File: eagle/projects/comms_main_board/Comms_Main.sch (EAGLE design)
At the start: 93 parts, among them J1 RECE-20279-001E, J2 PRT-12639, J3 PRT-12639, J4 PRT-12639, J5 PRT-12639, Q1 CSD17579Q3A, U1 TPS562209DDCT, U11 TPS562209DDCT, U2 LP2985-33DBVR, U3 LP5900TLX-3.3/NOPB, U4 TPS562209DDCT, U5 LMZ34002RKGR, U6 LM3488MMX/NOPB, U7 PCT2075D,118, U8 MS560702BA03-50, U9 MAX-M8Q

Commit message: Started comms connectors portion of schematic
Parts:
- added J6: MOL-KK-3P-RA, daqcs:MOLKK_3PIN_3RA_RA
- added J7: MOL-KK-5P-V, daqcs:MOLKK_5PIN_5RA_RA
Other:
- note added: "APRS I2C Connector"
- note added: "COMMS Connectors"
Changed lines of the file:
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@@
 <part name="R14" library="daqcs" deviceset="RES" device="_0603" technology="_0R0" value="0"/>
 <part name="R15" library="daqcs" deviceset="RES" device="_0603" technology="_0R0" value="0"/>
+<part name="J6" library="daqcs" deviceset="MOLKK_3PIN" device="_RA" technology="_3RA" value="MOL-KK-3P-RA"/>
+<part name="SUPPLY14" library="supply2" deviceset="GND" device=""/>
+<part name="J7" library="daqcs" deviceset="MOLKK_5PIN" device="_RA" technology="_5RA" value="MOL-KK-5P-V"/>
+<part name="SUPPLY15" library="supply2" deviceset="GND" device=""/>
 </parts>
 <sheets>
@@
 <sheet>
 <plain>
+<text x="-30.226" y="84.328" size="5.08" layer="91">COMMS Connectors</text>
+<text x="-110.49" y="46.99" size="1.778" layer="91">APRS I2C Connector</text>
 </plain>
 <instances>
 <instance part="FRAME7" gate="G$1" x="-129.54" y="-83.82"/>
+<instance part="J6" gate="G$1" x="-106.68" y="63.5"/>
+<instance part="SUPPLY14" gate="GND" x="-88.9" y="53.34"/>
+<instance part="J7" gate="G$1" x="-60.96" y="58.42"/>
+<instance part="SUPPLY15" gate="GND" x="-40.64" y="40.64"/>
 </instances>
 <busses>
 </busses>
 <nets>
+<net name="N$51" class="0">
+<segment>
+<wire x1="-94.234" y1="58.42" x2="-88.9" y2="58.42" width="0.1524" layer="91"/>
+<wire x1="-88.9" y1="58.42" x2="-88.9" y2="55.626" width="0.1524" layer="91"/>
+</segment>
+</net>
+<net name="SCL" class="0">
+<segment>
+<wire x1="-94.234" y1="63.5" x2="-81.026" y2="63.5" width="0.1524" layer="91"/>
+<label x="-91.44" y="63.5" size="1.778" layer="95"/>
+</segment>
+</net>
+<net name="SDA" class="0">
+<segment>
+<wire x1="-94.234" y1="68.58" x2="-81.026" y2="68.58" width="0.1524" layer="91"/>
+<label x="-91.44" y="68.58" size="1.778" layer="95"/>
+</segment>
+</net>
+<net name="GND" class="0">
+<segment>
+<pinref part="SUPPLY15" gate="GND" pin="GND"/>
+<wire x1="-48.768" y1="48.26" x2="-40.64" y2="48.26" width="0.1524" layer="91"/>
+<wire x1="-40.64" y1="48.26" x2="-40.64" y2="43.18" width="0.1524" layer="91"/>
+</segment>
+</net>
+<net name="MOSI" class="0">
+<segment>
+<wire x1="-48.768" y1="53.34" x2="-35.56" y2="53.34" width="0.1524" layer="91"/>
+<label x="-45.72" y="53.34" size="1.778" layer="95"/>
+</segment>
+</net>
+<net name="MISO" class="0">
+<segment>
+<wire x1="-49.022" y1="58.42" x2="-35.56" y2="58.42" width="0.1524" layer="91"/>
+<label x="-45.72" y="58.42" size="1.778" layer="95"/>
+</segment>
+</net>
+<net name="SCLK" class="0">
+<segment>
+<wire x1="-48.514" y1="63.5" x2="-35.56" y2="63.5" width="0.1524" layer="91"/>
+<label x="-45.72" y="63.5" size="1.778" layer="95"/>
+</segment>
+</net>
+<net name="SS" class="0">
+<segment>
+<wire x1="-48.514" y1="68.58" x2="-35.814" y2="68.58" width="0.1524" layer="91"/>
+<label x="-45.72" y="68.58" size="1.778" layer="95"/>
+</segment>
+</net>
 </nets>
 </sheet>

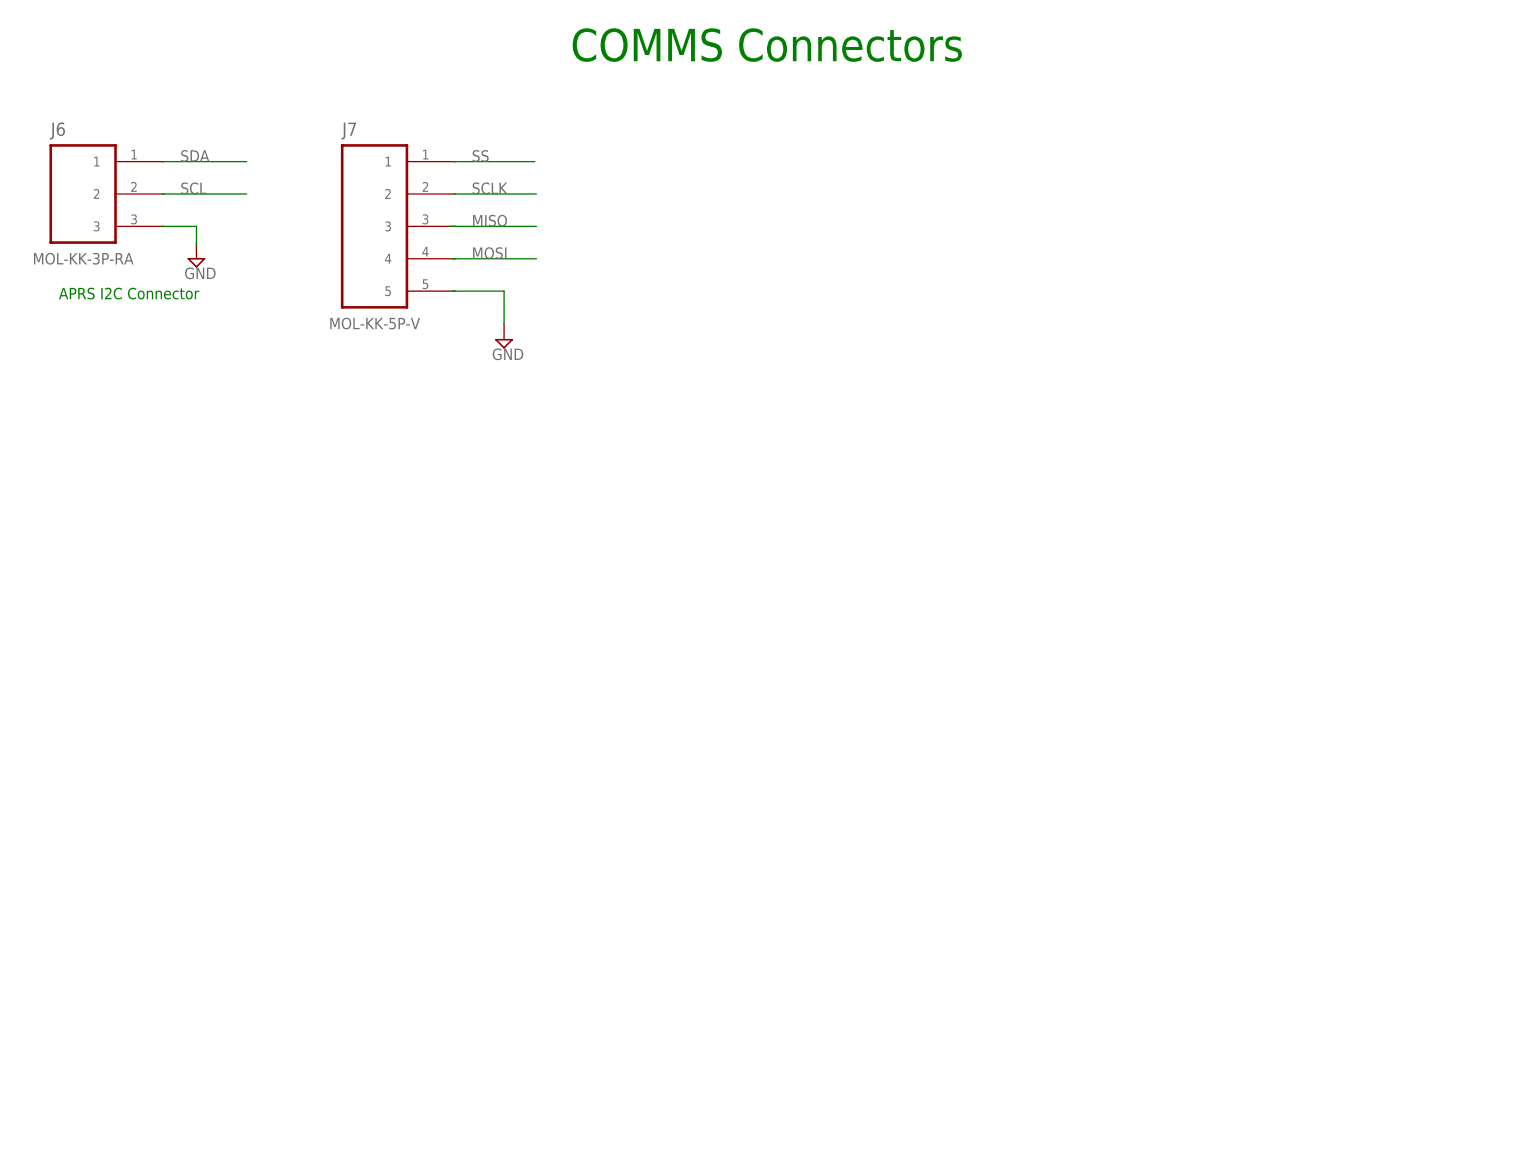
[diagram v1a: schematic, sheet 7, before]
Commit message: Added pi zero connector to schematic
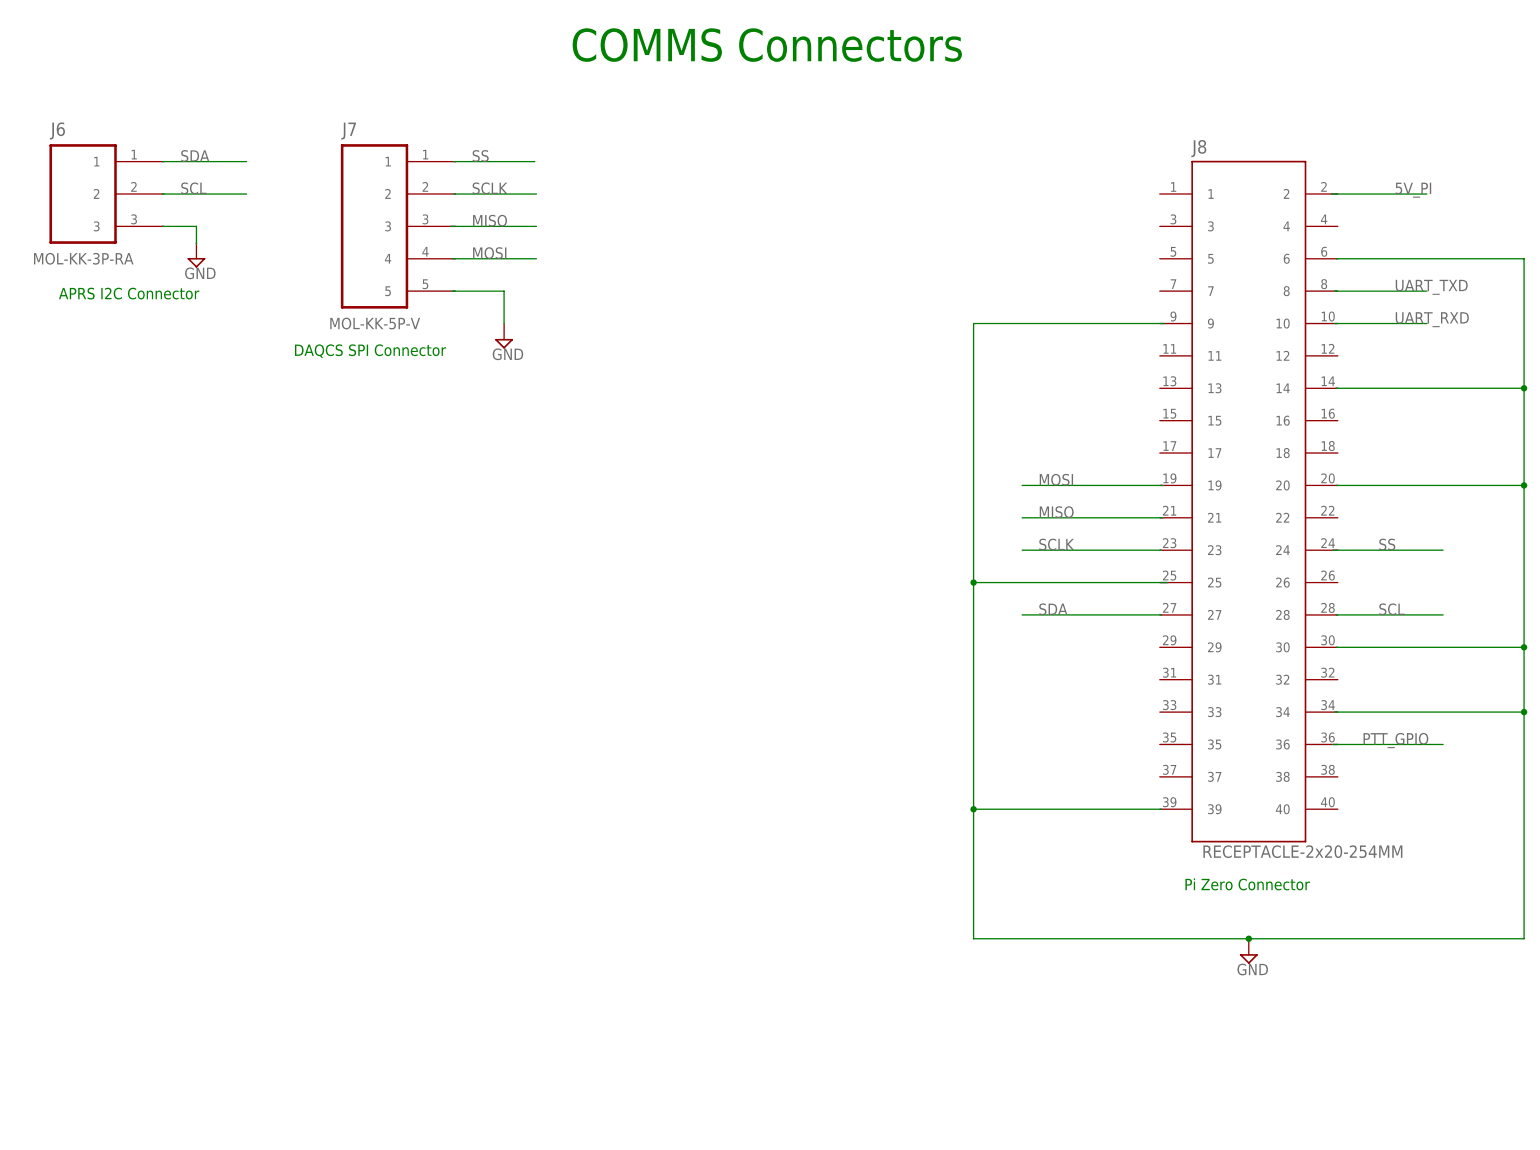
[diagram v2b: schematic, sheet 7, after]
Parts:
- added J8: RECEPTACLE-2x20-254MM, comms:RECEPTACLE-2X20-254MM
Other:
- note added: "DAQCS SPI Connector"
- note added: "Pi Zero Connector"
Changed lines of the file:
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@@
 <part name="J7" library="daqcs" deviceset="MOLKK_5PIN" device="_RA" technology="_5RA" value="MOL-KK-5P-V"/>
 <part name="SUPPLY15" library="supply2" deviceset="GND" device=""/>
+<part name="J8" library="comms" deviceset="RECEPTACLE-2X20-254MM" device="" value="RECEPTACLE-2x20-254MM"/>
+<part name="SUPPLY16" library="supply2" deviceset="GND" device=""/>
 </parts>
 <sheets>
@@
 <text x="-30.226" y="84.328" size="5.08" layer="91">COMMS Connectors</text>
 <text x="-110.49" y="46.99" size="1.778" layer="91">APRS I2C Connector</text>
+<text x="-73.66" y="38.1" size="1.778" layer="91">DAQCS SPI Connector</text>
+<text x="66.04" y="-45.72" size="1.778" layer="91">Pi Zero Connector</text>
 </plain>
 <instances>
@@
 <instance part="J7" gate="G$1" x="-60.96" y="58.42"/>
 <instance part="SUPPLY15" gate="GND" x="-40.64" y="40.64"/>
+<instance part="J8" gate="G$1" x="76.2" y="12.7"/>
+<instance part="SUPPLY16" gate="GND" x="76.2" y="-55.88"/>
 </instances>
 <busses>
@@
 <label x="-91.44" y="63.5" size="1.778" layer="95"/>
 </segment>
+<segment>
+<wire x1="89.916" y1="-2.54" x2="106.68" y2="-2.54" width="0.1524" layer="91"/>
+<label x="96.52" y="-2.54" size="1.778" layer="95"/>
+</segment>
 </net>
 <net name="SDA" class="0">
@@
 <wire x1="-94.234" y1="68.58" x2="-81.026" y2="68.58" width="0.1524" layer="91"/>
 <label x="-91.44" y="68.58" size="1.778" layer="95"/>
+</segment>
+<segment>
+<wire x1="62.484" y1="-2.54" x2="40.64" y2="-2.54" width="0.1524" layer="91"/>
+<label x="43.18" y="-2.54" size="1.778" layer="95"/>
 </segment>
 </net>
@@
 <wire x1="-40.64" y1="48.26" x2="-40.64" y2="43.18" width="0.1524" layer="91"/>
 </segment>
+<segment>
+<wire x1="62.992" y1="43.18" x2="33.02" y2="43.18" width="0.1524" layer="91"/>
+<wire x1="33.02" y1="43.18" x2="33.02" y2="2.54" width="0.1524" layer="91"/>
+<wire x1="33.02" y1="2.54" x2="63.5" y2="2.54" width="0.1524" layer="91"/>
+<wire x1="62.484" y1="-33.02" x2="33.02" y2="-33.02" width="0.1524" layer="91"/>
+<wire x1="33.02" y1="-33.02" x2="33.02" y2="2.54" width="0.1524" layer="91"/>
+<junction x="33.02" y="2.54"/>
+<pinref part="SUPPLY16" gate="GND" pin="GND"/>
+<wire x1="76.2" y1="-53.34" x2="33.02" y2="-53.34" width="0.1524" layer="91"/>
+<wire x1="33.02" y1="-53.34" x2="33.02" y2="-33.02" width="0.1524" layer="91"/>
+<junction x="33.02" y="-33.02"/>
+<wire x1="89.916" y1="53.34" x2="119.38" y2="53.34" width="0.1524" layer="91"/>
+<wire x1="89.916" y1="33.02" x2="119.38" y2="33.02" width="0.1524" layer="91"/>
+<wire x1="119.38" y1="33.02" x2="119.38" y2="53.34" width="0.1524" layer="91"/>
+<wire x1="89.916" y1="17.78" x2="119.38" y2="17.78" width="0.1524" layer="91"/>
+<wire x1="119.38" y1="17.78" x2="119.38" y2="33.02" width="0.1524" layer="91"/>
+<junction x="119.38" y="33.02"/>
+<wire x1="89.916" y1="-7.62" x2="119.38" y2="-7.62" width="0.1524" layer="91"/>
+<wire x1="119.38" y1="-7.62" x2="119.38" y2="17.78" width="0.1524" layer="91"/>
+<junction x="119.38" y="17.78"/>
+<wire x1="89.662" y1="-17.78" x2="119.38" y2="-17.78" width="0.1524" layer="91"/>
+<wire x1="119.38" y1="-17.78" x2="119.38" y2="-7.62" width="0.1524" layer="91"/>
+<junction x="119.38" y="-7.62"/>
+<wire x1="76.2" y1="-53.34" x2="119.38" y2="-53.34" width="0.1524" layer="91"/>
+<wire x1="119.38" y1="-53.34" x2="119.38" y2="-17.78" width="0.1524" layer="91"/>
+<junction x="76.2" y="-53.34"/>
+<junction x="119.38" y="-17.78"/>
+</segment>
 </net>
 <net name="MOSI" class="0">
@@
 <label x="-45.72" y="53.34" size="1.778" layer="95"/>
 </segment>
+<segment>
+<wire x1="62.738" y1="17.78" x2="40.64" y2="17.78" width="0.1524" layer="91"/>
+<label x="43.18" y="17.78" size="1.778" layer="95"/>
+</segment>
 </net>
 <net name="MISO" class="0">
@@
 <label x="-45.72" y="58.42" size="1.778" layer="95"/>
 </segment>
+<segment>
+<wire x1="62.738" y1="12.7" x2="40.64" y2="12.7" width="0.1524" layer="91"/>
+<label x="43.18" y="12.7" size="1.778" layer="95"/>
+</segment>
 </net>
 <net name="SCLK" class="0">
@@
 <label x="-45.72" y="63.5" size="1.778" layer="95"/>
 </segment>
+<segment>
+<wire x1="62.484" y1="7.62" x2="40.64" y2="7.62" width="0.1524" layer="91"/>
+<label x="43.18" y="7.62" size="1.778" layer="95"/>
+</segment>
 </net>
 <net name="SS" class="0">
@@
 <label x="-45.72" y="68.58" size="1.778" layer="95"/>
 </segment>
-</net>
+<segment>
+<wire x1="89.408" y1="7.62" x2="106.68" y2="7.62" width="0.1524" layer="91"/>
+<label x="96.52" y="7.62" size="1.778" layer="95"/>
+</segment>
+</net>
+<net name="5V_PI" class="0">
+<segment>
+<wire x1="89.154" y1="63.5" x2="104.14" y2="63.5" width="0.1524" layer="91"/>
+<label x="99.06" y="63.5" size="1.778" layer="95"/>
+</segment>
+</net>
+<net name="UART_TXD" class="0">
+<segment>
+<wire x1="89.662" y1="48.26" x2="104.14" y2="48.26" width="0.1524" layer="91"/>
+<label x="99.06" y="48.26" size="1.778" layer="95"/>
+</segment>
+</net>
+<net name="UART_RXD" class="0">
+<segment>
+<wire x1="89.662" y1="43.18" x2="104.14" y2="43.18" width="0.1524" layer="91"/>
+<label x="99.06" y="43.18" size="1.778" layer="95"/>
+</segment>
+</net>
+<net name="PTT_GPIO" class="0">
+<segment>
+<wire x1="89.408" y1="-22.86" x2="106.68" y2="-22.86" width="0.1524" layer="91"/>
+<label x="93.98" y="-22.86" size="1.778" layer="95"/>
+</segment>
+</net>
